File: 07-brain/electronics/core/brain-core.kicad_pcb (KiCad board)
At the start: 2 copper layers, 58 x 65 mm, 78 parts, among them J1 Conn_02x06_Odd_Even, J2 Conn_02x03_Odd_Even, J3 Conn_01x02, J4 Conn_02x04_Odd_Even, J5 Conn_02x02_Odd_Even, J6 Conn_02x05_Odd_Even, J7 Conn_02x05_Odd_Even, Q2 2N3819, Q4 BC848, U1 TL072, U2 TL072, U3 TL072, U4 NE5532, U5 TL072

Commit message: Design Brain/Core PCB
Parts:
- removed C17: 100n (foil), Capacitor_THT:C_Rect_L7.2mm_W2.5mm_P5.00mm_FKS2_FKP2_MKS2_MKP2
- removed C18: 1u (foil), Capacitor_THT:C_Rect_L7.0mm_W4.5mm_P5.00mm
- removed D_LIM_N1: Red LED, LED_THT:LED_D3.0mm
- removed D_LIM_P1: Red LED, LED_THT:LED_D5.0mm
- removed the G*** at (92.8, 84.6)
- removed the G*** at (82.2, 57.7)
- removed the J6 at (168.5, 98.0)
- removed Q2: 2N3819, Package_TO_SOT_THT:TO-92_Inline_Wide
- removed Q4: BC848, Package_TO_SOT_SMD:SOT-23
- removed the REF** at (125.1, 51.2)
- removed the REF** at (180.0, 87.8)
- removed RV_HEADPHONE_LIM1: 100k, Potentiometer_THT:Potentiometer_ACP_CA6-H2,5_Horizontal
- removed RV_LINE_OUT_LVL1: 10k, Potentiometer_THT:Potentiometer_ACP_CA6-H2,5_Horizontal
- removed TP1: MAX_LINEOUT, TestPoint:TestPoint_THTPad_2.0x2.0mm_Drill1.0mm
- removed TP2: MAINOUT, TestPoint:TestPoint_THTPad_2.0x2.0mm_Drill1.0mm
- removed TP3: PHONES_OUT, TestPoint:TestPoint_THTPad_2.0x2.0mm_Drill1.0mm
- added D5: BAT54S, Package_TO_SOT_SMD:SOT-23, F.Cu at (161.3, 88.1)
- added D6: BAT54S, Package_TO_SOT_SMD:SOT-23, F.Cu at (168.0, 88.0)
- added G***: LOGO, Shmoergh_Logo:Gyeszno, F.Cu at (202.0, 31.0)
- added G***: LOGO, Shmoergh_Logo:Gyeszno, B.Cu at (105.0, 126.0)
- added J10: Conn_01x02, Connector_PinHeader_2.54mm:PinHeader_1x02_P2.54mm_Vertical, F.Cu at (180.0, 52.6)
- added J7: Conn_02x05_Odd_Even, Connector_PinHeader_2.54mm:PinHeader_2x05_P2.54mm_Vertical, F.Cu at (161.0, 96.5)
- added J8: Conn_02x03_Odd_Even, Connector_PinHeader_2.54mm:PinHeader_2x03_P2.54mm_Vertical, F.Cu at (136.0, 152.0)
- added NT1: NetTie_2, NetTie:NetTie-2_SMD_Pad2.0mm, F.Cu at (160.2, 79.6)
- added Q1: MMBT3904, Package_TO_SOT_SMD:SOT-23, F.Cu at (175.1, 58.0)
- added Q3: MMBT3904, Package_TO_SOT_SMD:SOT-23, F.Cu at (171.0, 53.8)
- added Q6: MMBT3904, Package_TO_SOT_SMD:SOT-23, F.Cu at (163.9, 48.3)
- added Q7: MMBT3904, Package_TO_SOT_SMD:SOT-23, F.Cu at (159.1, 47.9)
- added R28: 33k, Resistor_SMD:R_0603_1608Metric, F.Cu at (139.8, 111.3)
- added R29: 33k, Resistor_SMD:R_0603_1608Metric, F.Cu at (155.0, 111.5)
- added R30: 100k, Resistor_SMD:R_0603_1608Metric, F.Cu at (149.8, 114.4)
- added R31: 100k, Resistor_SMD:R_0603_1608Metric, F.Cu at (165.1, 114.6)
- added R32: 100k, Resistor_SMD:R_0603_1608Metric, F.Cu at (149.8, 112.8)
- added R33: 100k, Resistor_SMD:R_0603_1608Metric, F.Cu at (165.1, 113.0)
- added R34: 1k, Resistor_SMD:R_0603_1608Metric, F.Cu at (149.8, 111.1)
- added R35: 1k, Resistor_SMD:R_0603_1608Metric, F.Cu at (165.1, 111.4)
- added REF**: ToolingHole_1.152mm, MountingHole:ToolingHole_1.152mm, F.Cu at (117.0, 110.0)
- added REF**: ToolingHole_1.152mm, MountingHole:ToolingHole_1.152mm, F.Cu at (116.9, 113.0)
- added REF**: ToolingHole_1.152mm, MountingHole:ToolingHole_1.152mm, F.Cu at (120.0, 110.0)
- added U10: 74HC4051, Package_SO:SOIC-16_3.9x9.9mm_P1.27mm, F.Cu at (154.1, 90.1)
- added U6: MCP4822, Package_SO:SOIC-8_3.9x4.9mm_P1.27mm, F.Cu at (129.1, 122.4)
- added U7: 74HC4053B, Package_SO:SOIC-16_3.9x9.9mm_P1.27mm, F.Cu at (133.3, 111.9)
- added U8: TL072, Package_SO:SOIC-8_3.9x4.9mm_P1.27mm, F.Cu at (144.5, 112.8)
- added U9: TL072, Package_SO:SOIC-8_3.9x4.9mm_P1.27mm, F.Cu at (159.7, 112.8)
- C1: value 100n -> 10u; footprint Capacitor_SMD:C_0603_1608Metric -> Capacitor_SMD:CP_Elec_4x5.4
- C10, C11: value 100n -> 22p
- C14: value 1u -> 100n; footprint Capacitor_SMD:C_0603_1608Metric_Pad1.08x0.95mm_HandSolder -> Capacitor_SMD:C_0603_1608Metric
- C15: value 100p -> 100n
- C16: value 100n (foil) -> 100n; footprint Capacitor_THT:C_Rect_L7.2mm_W2.5mm_P5.00mm_FKS2_FKP2_MKS2_MKP2 -> Capacitor_SMD:C_0603_1608Metric
- C2: value 100n -> 330n; footprint Capacitor_SMD:C_0603_1608Metric -> Capacitor_SMD:C_0603_1608Metric_Pad1.08x0.95mm_HandSolder
- C4, C5: value 100n -> 100u; footprint Capacitor_SMD:C_0603_1608Metric -> Capacitor_SMD:CP_Elec_6.3x7.7
- C7: value 22n-47n (foil) -> 100n; footprint Capacitor_THT:C_Rect_L7.0mm_W2.5mm_P5.00mm -> Capacitor_SMD:C_0603_1608Metric
- C8, C9: value 100u -> 100n; footprint Capacitor_SMD:CP_Elec_6.3x7.7 -> Capacitor_SMD:C_0603_1608Metric
- D3: value 1N4148 -> 1N5817; footprint Diode_SMD:D_SOD-123 -> Diode_SMD:D_SOD-323
- D4: value 1N4148 -> BAT54W; footprint Diode_SMD:D_SOD-123 -> Package_TO_SOT_SMD:SOT-23
- J1: value Conn_02x06_Odd_Even -> Conn_02x03_Odd_Even; footprint Connector_PinHeader_2.54mm:PinHeader_2x06_P2.54mm_Vertical -> Connector_PinHeader_2.54mm:PinHeader_2x03_P2.54mm_Vertical
- J2: value Conn_02x03_Odd_Even -> Conn_02x02_Odd_Even; footprint Connector_PinHeader_2.54mm:PinHeader_2x03_P2.54mm_Vertical -> Connector_PinHeader_2.54mm:PinHeader_2x02_P2.54mm_Vertical
- J3: value Conn_01x02 -> Conn_02x02_Odd_Even; footprint Connector_PinHeader_2.54mm:PinHeader_1x02_P2.54mm_Vertical -> Connector_PinHeader_2.54mm:PinHeader_2x02_P2.54mm_Vertical
- J4: value Conn_02x04_Odd_Even -> Conn_02x03_Odd_Even; footprint Connector_PinHeader_2.54mm:PinHeader_2x04_P2.54mm_Vertical -> Connector_PinHeader_2.54mm:PinHeader_2x03_P2.54mm_Vertical
- J5: value Conn_02x02_Odd_Even -> Conn_01x02; footprint Connector_PinHeader_2.54mm:PinHeader_2x02_P2.54mm_Vertical -> Connector_PinHeader_2.54mm:PinHeader_1x02_P2.54mm_Vertical
- R1: value 33k -> 100k
- R10: value 100k -> 68k; footprint Resistor_SMD:R_0603_1608Metric_Pad0.98x0.95mm_HandSolder -> Resistor_SMD:R_0603_1608Metric
- R11: value 4.7k -> 68k
- R12: value 150 -> 1k
- R14, R15: value 100 -> 100k
- R16: value 1M -> 100k
- R17: value 1k -> 100k
- R18, R20: value 10k -> 100k
- R22, R23: value 100k -> 1k
- R24: value 47k -> 100k
- R25: value 1k -> 120k
- R26: value 12k -> 100k
- R27: value 47k -> 120k
- R3: value 100k -> 10k
- R4: value 100k -> 7.5k
- R5: value 100k -> 2.2k
- R6: value 100k -> 120
- U1: value TL072 -> LM7805_TO220; footprint Package_SO:SOIC-8_3.9x4.9mm_P1.27mm -> Package_TO_SOT_THT:TO-220-3_Horizontal_TabDown
- U2: value TL072 -> 6N137; footprint Package_SO:SOIC-8_3.9x4.9mm_P1.27mm -> Package_SO:SOP-8_6.605x9.655mm_P2.54mm
- U3: value TL072 -> Pico; footprint Package_SO:SOIC-8_3.9x4.9mm_P1.27mm -> Module:RaspberryPi_Pico_Common_Unspecified
- U4: value NE5532 -> TL072
- moved J5 102.9 mm to (152.1, 148.9)
- moved C7 97.9 mm to (128.6, 133.2), turned to -90 degrees
- moved C4 91.8 mm to (159.8, 150.3), turned to 180 degrees
- moved C6 83.9 mm to (135.2, 140.9), turned to -90 degrees
- moved R18 81.3 mm to (145.8, 143.5)
- moved R8 80.9 mm to (132.5, 131.6), turned to -90 degrees
- moved D2 78.0 mm to (158.9, 144.5)
- moved R16 76.9 mm to (128.2, 142.7), turned to 90 degrees
- moved R9 75.4 mm to (145.5, 130.0), turned to -90 degrees
- moved R23 74.3 mm to (148.6, 144.3)
- moved R22 68.2 mm to (135.2, 144.2), turned to -90 degrees
- moved R21 68.1 mm to (145.8, 141.9), turned to 0 degrees
- moved C9 68.0 mm to (141.9, 133.2), turned to -90 degrees
- moved J4 68.0 mm to (168.0, 152.0), turned to 90 degrees
- moved C5 66.9 mm to (176.8, 120.7), turned to 180 degrees
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- renumbered J7 to J6
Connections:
- C10 pad 1: +12V -> Net-(U4A--)
- C10 pad 2: GND -> Net-(C10-Pad2)
- C11 pad 1: GND -> Net-(U5A--)
- C11 pad 2: -12V -> Net-(C11-Pad2)
- C12 pad 2: GND -> GNDA
- C13 pad 1: GND -> GNDA
- C14 pad 1: OUTPUT_VOL_2 -> +12V
- C14 pad 2: Net-(U5A-+) -> GNDA
- C15 pad 1: Net-(U5B--) -> GNDA
- C15 pad 2: OUTPUT_LINE_OUT -> -12V
- C16 pad 1: Net-(Q2-S) -> +3.3V
- C16 pad 2: GND -> GNDA
- C2 pad 1: GND -> +12V
- C2 pad 2: -12V -> GND
- C3 pad 1: +12V -> Net-(D1-A)
- C4 pad 1: GND -> +12V
- C4 pad 2: -12V -> GND
- C5 pad 1: +12V -> GND
- C5 pad 2: GND -> -12V
- C6 pad 1: GND -> +12V
- C6 pad 2: -12V -> GNDA
- C7 pad 1: LFO_TRI -> GNDA
- C7 pad 2: Net-(U3A--) -> -12V
- C8 pad 2: GND -> GNDA
- C9 pad 1: GND -> GNDA
- D1 pad 1: +12V -> +5V
- D2 pad 1: Net-(D2-K) -> +12V
- D2 pad 2: -12V -> Net-(D2-A)
- D3 pad 2: Net-(D3-A) -> -12V
- D4 pad 1: Net-(D4-K) -> MIDI_4R
- D4 pad 2: Net-(D4-A) -> unconnected-(D4-NC-Pad2)
- J1 pad 1: Net-(J1-Pin_1) -> LED_3
- J1 pad 2: Net-(J1-Pin_1) -> LED_4
- J1 pad 3: Net-(J1-Pin_3) -> LED_2
- J1 pad 4: Net-(J1-Pin_3) -> LED_5
- J1 pad 5: Net-(J1-Pin_5) -> LED_1
- J1 pad 6: Net-(J1-Pin_5) -> LED_6
- J2 pad 1: GND -> MIDI_5T
- J2 pad 2: +12V -> PULSE_IN
- J2 pad 3: GND -> MIDI_4R
- J2 pad 4: GND -> PULSE_OUT
- J3 pad 1: GND -> BTN_2
- J3 pad 2: GND -> BTN_LED_1
- J4 pad 1: CRUSH_OUT -> GND
- J4 pad 2: CRUSH_IN -> +12V
- J4 pad 3: CRUSH_TRIG -> GND
- J4 pad 4: CRUSH_TRIG_DEFAULT -> GND
- J4 pad 5: RV_CRUSH_1 -> -12V
- J4 pad 6: RV_CRUSH_3 -> GND
- J5 pad 1: LFO_SQR -> GND
- J5 pad 2: LFO_TRI -> GND
- J6 pad 1: Net-(D2-K) -> Net-(D3-K)
- J6 pad 10: Net-(D1-A) -> Net-(D2-A)
- J6 pad 2: Net-(D2-K) -> Net-(D3-K)
- J6 pad 9: Net-(D1-A) -> Net-(D2-A)
- R1 pad 1: GND -> PULSE_IN
- R1 pad 2: Net-(U2B--) -> Net-(Q1-B)
- R10 pad 1: GND -> Net-(U4A--)
- R10 pad 2: Net-(U5A-+) -> Net-(R10-Pad2)
- R11 pad 1: OUTPUT_LINE_OUT -> Net-(U5A--)
- R11 pad 2: Net-(U5B--) -> Net-(R11-Pad2)
- R12 pad 1: OUTPUT_LINE_OUT -> Net-(C10-Pad2)
- R12 pad 2: Net-(R12-Pad2) -> Net-(R10-Pad2)
- R13 pad 1: OUTPUT_LINE_OUT -> Net-(C11-Pad2)
- R13 pad 2: Net-(R13-Pad2) -> Net-(R11-Pad2)
- R14 pad 1: OUTPUT_PHONES_OUT -> Net-(R10-Pad2)
- R14 pad 2: Net-(U4B--) -> Net-(U4B-+)
- R15 pad 1: OUTPUT_PHONES_OUT -> Net-(R11-Pad2)
- R15 pad 2: Net-(U4A--) -> Net-(U5B-+)
- R16 pad 1: Net-(D4-A) -> GNDA
- R16 pad 2: Net-(Q2-D) -> Net-(U4B-+)
- R17 pad 1: Net-(U1B--) -> GNDA
- R17 pad 2: CRUSH_OUT -> Net-(U5B-+)
- R18 pad 1: Net-(U2A--) -> Net-(U7-A)
- R18 pad 2: CRUSH_TRIG_DEFAULT -> Net-(U5B--)
- R19 pad 1: RV_CRUSH_3 -> Net-(U4B--)
- R19 pad 2: CRUSH_TRIG_DEFAULT -> Net-(U7-B)
- R2 pad 1: LFO_RATE -> /GPIO_8
- R2 pad 2: Net-(U3A--) -> Net-(Q3-B)
- R20 pad 1: GND -> Net-(U4B--)
- R20 pad 2: RV_CRUSH_1 -> Net-(R20-Pad2)
- R21 pad 1: GND -> Net-(U5B--)
- R21 pad 2: Net-(D3-A) -> Net-(R21-Pad2)
- R22 pad 1: Net-(U2B--) -> Net-(R20-Pad2)
- R22 pad 2: +12V -> AUDIO_CV_OUT_2
- R23 pad 1: GND -> Net-(R21-Pad2)
- R23 pad 2: Net-(D3-K) -> AUDIO_CV_OUT_1
- R24 pad 1: GND -> +5V
- R24 pad 2: OUTPUT_DRIVE_1 -> Net-(U8A--)
- R25 pad 1: Net-(D_LIM_N1-K) -> AUDIO_CV_IN_1
- R25 pad 2: OUTPUT_DRIVE_3 -> Net-(U8A--)
- R26 pad 1: Net-(R26-Pad1) -> +5V
- R26 pad 2: LFO_SQR -> Net-(U9A--)
- R27 pad 1: LFO_SQR -> AUDIO_CV_IN_2
- R27 pad 2: GND -> Net-(U9A--)
- R3 pad 1: Net-(U3A-+) -> PULSE_OUT
- R3 pad 2: LFO_RATE -> +12V
- R4 pad 1: Net-(Q4-C) -> GND
- R4 pad 2: Net-(U3A--) -> PULSE_OUT
- R5 pad 1: Net-(U3A--) -> Net-(Q6-C)
- R5 pad 2: Net-(Q4-C) -> Net-(D4-K)
- R6 pad 1: Net-(U3A-+) -> MIDI_5T
- R6 pad 2: GND -> Net-(Q6-B)
- R7 pad 1: Net-(R26-Pad1) -> /GPIO_9
- R7 pad 2: Net-(Q4-B) -> +3.3V
- R8 pad 1: Net-(U3B-+) -> GNDA
- R8 pad 2: GND -> Net-(U4A--)
- R9 pad 1: Net-(U3B-+) -> GNDA
- R9 pad 2: Net-(R26-Pad1) -> Net-(U5A--)
- U1 pad 1: Net-(Q2-D) -> +12V
- U1 pad 2: Net-(Q2-D) -> GND
- U1 pad 3: CRUSH_IN -> Net-(D1-A)
- U2 pad 1: CRUSH_TRIG_DEFAULT -> unconnected-(U2-NC-Pad1)
- U2 pad 2: Net-(U2A--) -> Net-(D4-K)
- U2 pad 3: RV_CRUSH_2 -> Net-(Q7-C)
- U2 pad 4: -12V -> unconnected-(U2-NC-Pad4)
- U2 pad 5: Net-(D3-K) -> GND
- U2 pad 6: Net-(U2B--) -> /GPIO_9
- U2 pad 7: Net-(D4-K) -> unconnected-(U2-EN-Pad7)
- U2 pad 8: +12V -> +3.3V
- U3 pad 1: LFO_TRI -> /MCU/UART_TX
- U3 pad 2: Net-(U3A--) -> /MCU/UART_RX
- U3 pad 3: Net-(U3A-+) -> GND
- U3 pad 4: -12V -> /GPIO_2
- U3 pad 5: Net-(U3B-+) -> /GPIO_3
- U3 pad 6: LFO_TRI -> /GPIO_4
- U3 pad 7: Net-(R26-Pad1) -> /GPIO_5
- U3 pad 8: +12V -> GND
- U4 pad 1: Net-(U4A--) -> Net-(C10-Pad2)
- U4 pad 5: Net-(U4A--) -> Net-(U4B-+)
- U4 pad 7: Net-(U4B--) -> Net-(R20-Pad2)
- U5 pad 1: OUTPUT_DRIVE_3 -> Net-(C11-Pad2)
- U5 pad 2: OUTPUT_DRIVE_1 -> Net-(U5A--)
- U5 pad 5: Net-(D_LIM_N1-K) -> Net-(U5B-+)
- U5 pad 7: Net-(R12-Pad2) -> Net-(R21-Pad2)
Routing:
- net +3.3V: track 0.00 -> 118.4 mm, vias 0 -> 10
- net /GPIO_2: track 0.00 -> 101.2 mm
- net /GPIO_3: track 0.00 -> 99.7 mm
- net +5V: track 0.00 -> 95.1 mm, vias 0 -> 4
- net /GPIO_5: track 0.00 -> 93.8 mm, vias 0 -> 1
- net /GPIO_6: track 0.00 -> 73.0 mm, vias 0 -> 1
- net CRUSH_TRIG_DEFAULT: track 68.6 -> 0.00 mm
- net /GPIO_7: track 0.00 -> 67.7 mm, vias 0 -> 1
- net Net-(U7-A): track 0.00 -> 63.9 mm, vias 0 -> 6
- net Net-(D_LIM_N1-K): track 62.1 -> 0.00 mm, vias 4 -> 0
- net OUTPUT_DRIVE_3: track 52.6 -> 0.00 mm, vias 2 -> 0
- net /GPIO_17: track 0.00 -> 47.0 mm
- net Net-(U7-B): track 0.00 -> 46.5 mm, vias 0 -> 2
- net /GPIO_16: track 0.00 -> 46.2 mm
- net RV_CRUSH_2: track 44.4 -> 0.00 mm
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- added copper zone on F.Cu, net GNDA
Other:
- board size 58 x 65 mm -> 58 x 110 mm
- board text added: "12V has to be connected on the UI board (or manually here)"
- board text added: "HM-02 Analog VCO Core V0.1 / 2025 July"
- board text removed: "+"
- board text removed: "12V"
- board text removed: "DEFAULTS"
- board text removed: "ENV"
- board text removed: "ENV GAIN"
- board text removed: "GATE"
- board text removed: "HM-05 ADSR VCA V0.1 / 2025 Aug"
- board text removed: "NC"
- board text removed: "TP(2xGND)"
- board text removed: "VCA COMP"
- board text removed: "VCV"
- board text removed: "VIN"
- board text removed: "VOUT"

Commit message: Brain PCB WIP
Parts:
- removed NT1: NetTie_2, NetTie:NetTie-2_SMD_Pad2.0mm
- moved J10 25.8 mm to (155.0, 46.0), turned to -90 degrees
- moved U6 19.0 mm to (139.9, 106.7)
- moved R25 15.4 mm to (150.8, 102.5)
- moved R19 8.89 mm to (128.1, 135.8)
- moved U7 5.63 mm to (131.4, 106.7), turned to 90 degrees
- moved U8 4.63 mm to (148.2, 115.5)
- moved C15 4.63 mm to (159.6, 118.9)
- moved R24 4.63 mm to (148.4, 111.1)
- moved R26 4.63 mm to (163.1, 111.1)
- moved R32 4.63 mm to (153.6, 115.5)
- moved U9 4.63 mm to (163.4, 115.5)
- moved C12 4.63 mm to (152.1, 112.0)
- moved C13 4.63 mm to (144.4, 118.8)
- moved C14 4.63 mm to (167.3, 112.1)
- moved R27 4.63 mm to (157.1, 114.2)
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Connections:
- C12 pad 2: GNDA -> GND
- C13 pad 1: GNDA -> GND
- C14 pad 2: GNDA -> GND
- C15 pad 1: GNDA -> GND
- C16 pad 2: GNDA -> GND
- C6 pad 2: GNDA -> GND
- C7 pad 1: GNDA -> GND
- C8 pad 2: GNDA -> GND
- C9 pad 1: GNDA -> GND
- D5 pad 1: GNDA -> GND
- D6 pad 1: GNDA -> GND
- J10 pad 2: +12V -> +3.3V
- R16 pad 1: GNDA -> GND
- R17 pad 1: GNDA -> GND
- R8 pad 1: GNDA -> GND
- R9 pad 1: GNDA -> GND
- U10 pad 1: GNDA -> GND
- U10 pad 12: GNDA -> GND
- U10 pad 2: GNDA -> GND
- U10 pad 4: GNDA -> GND
- U10 pad 5: GNDA -> GND
- U10 pad 6: GNDA -> GND
- U10 pad 7: GNDA -> GND
- U10 pad 8: GNDA -> GND
- U10 pad 9: GNDA -> GND
- U3 pad 33: GNDA -> GND
- U6 pad 5: GNDA -> GND
- U6 pad 7: GNDA -> GND
- U7 pad 12: GNDA -> GND
- U7 pad 2: GNDA -> GND
- U7 pad 3: GNDA -> GND
- U7 pad 4: GNDA -> GND
- U7 pad 5: GNDA -> GND
- U7 pad 6: GNDA -> GND
- U7 pad 7: GNDA -> GND
- U7 pad 8: GNDA -> GND
- U7 pad 9: GNDA -> GND
- U8 pad 3: GNDA -> GND
- U8 pad 5: GNDA -> GND
- U9 pad 3: GNDA -> GND
- U9 pad 5: GNDA -> GND
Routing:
- net GNDA: track 29.2 -> 0.00 mm, vias 14 -> 0
- net +12V: track 162.8 -> 190.7 mm, vias 3 -> 4
- net /GPIO_5: track 93.8 -> 72.5 mm
- net /GPIO_3: track 99.7 -> 78.8 mm
- net /GPIO_2: track 101.2 -> 80.7 mm
- net AUDIO_CV_IN_1: track 21.7 -> 2.70 mm
- net Net-(U4A-+): track 10.8 -> 27.0 mm
- net Net-(U7-A): track 63.9 -> 74.6 mm, vias 6 -> 2
- net Net-(U8A--): track 9.28 -> 18.0 mm
- net /GPIO_17: track 47.0 -> 38.7 mm
- net Net-(U7-B): track 46.5 -> 38.4 mm, vias 2 -> 0
- net /GPIO_16: track 46.2 -> 38.6 mm
- net -12V: track 130.7 -> 123.3 mm
- net /GPIO_7: track 67.7 -> 73.2 mm
- net Net-(U5A-+): track 21.4 -> 26.7 mm
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- removed copper zone on F.Cu, net GNDA

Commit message: Designed Brain UI PCB
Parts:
- added J_USB_C_BRKOUT1: Conn_01x05, Connector_PinHeader_2.54mm:PinHeader_1x05_P2.54mm_Vertical, F.Cu at (167.7, 68.3)
- added SW1: SW_SPST, Button_Switch_THT:SW_Tactile_SKHH_Angled, F.Cu at (179.1, 53.5)
- U3: moved to B.Cu
- moved R3 48.1 mm to (126.9, 54.7), turned to 180 degrees
- moved R4 48.1 mm to (126.9, 53.0), turned to 0 degrees
- moved D1 42.8 mm to (133.8, 90.7), turned to -90 degrees
- moved Q3 41.2 mm to (129.9, 56.7)
- moved J5 40.8 mm to (126.5, 117.0)
- moved C3 36.9 mm to (134.5, 95.0)
- moved U1 36.9 mm to (141.8, 94.2)
- moved C1 36.9 mm to (140.0, 89.9)
- moved C2 36.9 mm to (144.1, 93.3)
- moved R1 35.6 mm to (139.0, 52.8)
- moved Q1 34.0 mm to (141.1, 56.3), turned to 0 degrees
- moved J10 31.2 mm to (126.0, 57.5), turned to 0 degrees
- moved J2 27.1 mm to (141.5, 49.0), turned to 180 degrees
- moved J1 25.6 mm to (165.0, 49.5), turned to 90 degrees
- moved R28 24.3 mm to (167.3, 109.3)
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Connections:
- J1 pad 1: LED_3 -> LED_1
- J1 pad 2: LED_4 -> LED_6
- J1 pad 5: LED_1 -> LED_3
- J1 pad 6: LED_6 -> LED_4
- J3 pad 1: BTN_2 -> BTN_1
- J3 pad 2: BTN_LED_1 -> BTN_LED_2
- J3 pad 3: BTN_1 -> BTN_2
- J3 pad 4: BTN_LED_2 -> BTN_LED_1
- J7 pad 1: POT_3 -> POT_2
- J7 pad 10: AUDIO_CV_IN_1 -> AUDIO_CV_IN_2
- J7 pad 2: GND -> POT_3
- J7 pad 3: POT_2 -> POT_1
- J7 pad 5: POT_1 -> GND
- J7 pad 6: AUDIO_CV_IN_2 -> AUDIO_CV_IN_1
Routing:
- net /GPIO_26: track 5.31 -> 43.5 mm
- net +3.3V: track 119.0 -> 153.9 mm, vias 10 -> 4
- net /GPIO_17: track 38.7 -> 10.4 mm
- net +12V: track 190.7 -> 162.9 mm
- net Net-(U7-A): track 74.6 -> 48.4 mm, vias 2 -> 4
- net /GPIO_16: track 38.6 -> 13.1 mm
- net LED_1: track 33.4 -> 15.8 mm
- net Net-(U4A-+): track 27.0 -> 9.77 mm
- net LED_6: track 16.6 -> 33.8 mm
- net Net-(Q3-B): track 10.1 -> 26.8 mm
- net /GPIO_2: track 80.7 -> 66.6 mm
- net BTN_2: track 9.59 -> 22.7 mm
- net BTN_1: track 14.4 -> 27.3 mm
- net BTN_LED_1: track 9.59 -> 22.0 mm
- net /GPIO_7: track 73.2 -> 85.5 mm, vias 1 -> 0
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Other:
- board text added: "Adafruit 5978 USB-C breakout soldered to TP pads on Pico. TBD"
- board text added: "Bootsel button, soldered to TP pads on the Pico. TBD"
- board text added: "Pico should be soldered top facing downwards using low profile pin sockets and headers. This way the bootsel button is accessible and the USB-C breakout can be attached to TP pads."

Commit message: Added decoupling caps to DAC in Brain
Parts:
- added C17: 100n, Capacitor_SMD:C_0603_1608Metric, F.Cu at (135.0, 115.8)
- added C18: 10u, Capacitor_SMD:C_0603_1608Metric, F.Cu at (137.7, 115.4)
- J_USB_C_BRKOUT1: value Conn_01x05 -> Conn_02x05_Top_Bottom; footprint Connector_PinHeader_2.54mm:PinHeader_1x05_P2.54mm_Vertical -> Connector_PinHeader_2.54mm:PinHeader_2x05_P2.54mm_Vertical
- moved J_USB_C_BRKOUT1 2.71 mm to (165.0, 68.6)
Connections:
- J_USB_C_BRKOUT1 pad 1: unconnected-(J_USB_C_BRKOUT1-Pin_1-Pad1) -> Net-(J_USB_C_BRKOUT1-Pin_1)
- J_USB_C_BRKOUT1 pad 2: unconnected-(J_USB_C_BRKOUT1-Pin_2-Pad2) -> Net-(J_USB_C_BRKOUT1-Pin_1)
- J_USB_C_BRKOUT1 pad 3: unconnected-(J_USB_C_BRKOUT1-Pin_3-Pad3) -> Net-(J_USB_C_BRKOUT1-Pin_3)
- J_USB_C_BRKOUT1 pad 4: unconnected-(J_USB_C_BRKOUT1-Pin_4-Pad4) -> Net-(J_USB_C_BRKOUT1-Pin_3)
- J_USB_C_BRKOUT1 pad 5: unconnected-(J_USB_C_BRKOUT1-Pin_5-Pad5) -> Net-(J_USB_C_BRKOUT1-Pin_5)
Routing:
- net Net-(J_USB_C_BRKOUT1-Pin_7): track 0.00 -> 2.54 mm
- net Net-(J_USB_C_BRKOUT1-Pin_5): track 0.00 -> 2.54 mm
- net Net-(J_USB_C_BRKOUT1-Pin_3): track 0.00 -> 2.54 mm
- net Net-(J_USB_C_BRKOUT1-Pin_10): track 0.00 -> 2.54 mm
- net Net-(J_USB_C_BRKOUT1-Pin_1): track 0.00 -> 2.54 mm
- net GND: vias 50 -> 52

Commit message: Refined Brain PCBs
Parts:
- added G***: LOGO, Shmoergh_Logo:Gyeszno, F.Cu at (128.8, 108.6)
- added J9: Conn_01x02, Connector_PinHeader_2.54mm:PinHeader_1x02_P2.54mm_Vertical, F.Cu at (134.8, 90.6)
- moved G*** 99.8 mm to (159.6, 121.3)
- moved D1 2.75 mm to (131.9, 88.7)
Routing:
- net +12V: track 162.9 -> 173.9 mm
- net Net-(D1-A): track 5.23 -> 8.67 mm
- net +5V: track 103.1 -> 102.4 mm
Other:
- board text added: "(2x)+12V"
- board text added: "(2x)GND"
- board text added: "+12V"
- board text added: "3.3V"
- board text added: "Adafruit 5978 USB-C breakout"
- board text added: "BOOTSEL button"
- board text added: "Connect +12V here OR on the UI board (used for Pulse out)."

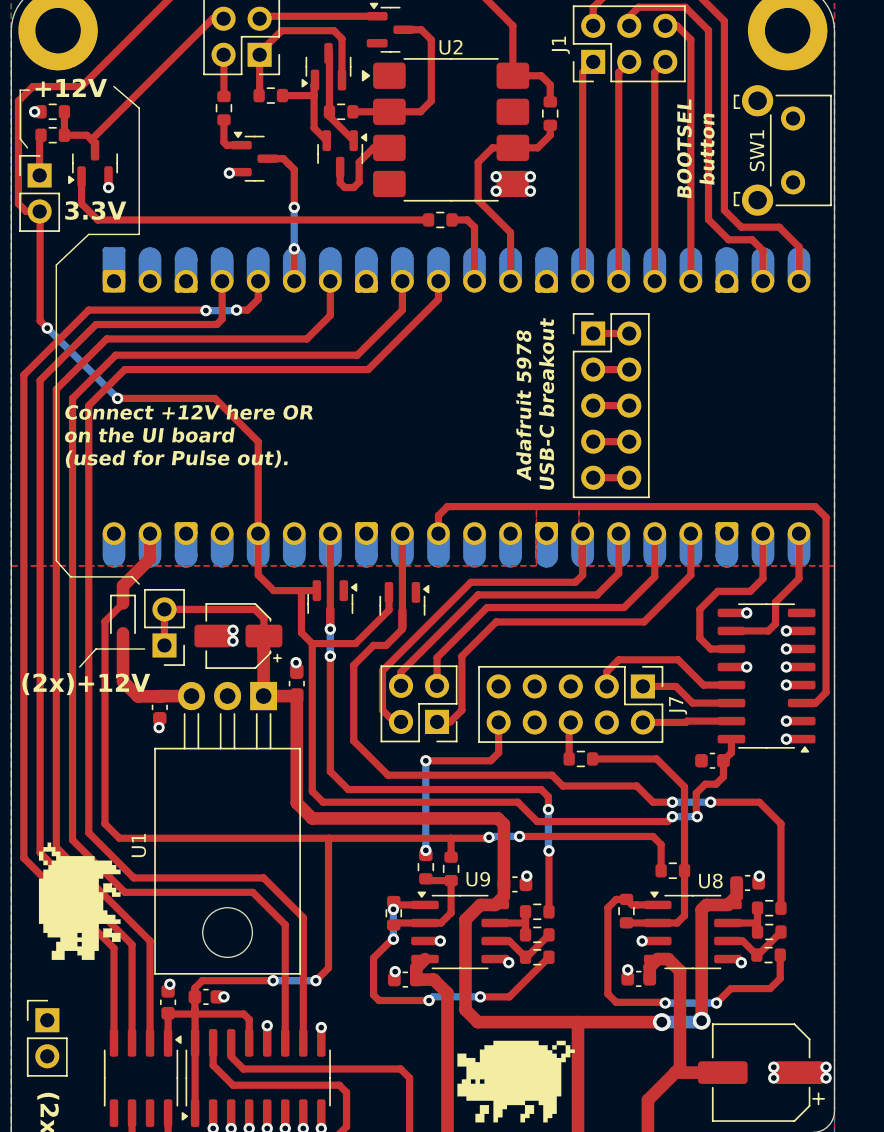
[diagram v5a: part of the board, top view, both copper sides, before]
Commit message: Added Adafruit USB-C breakout
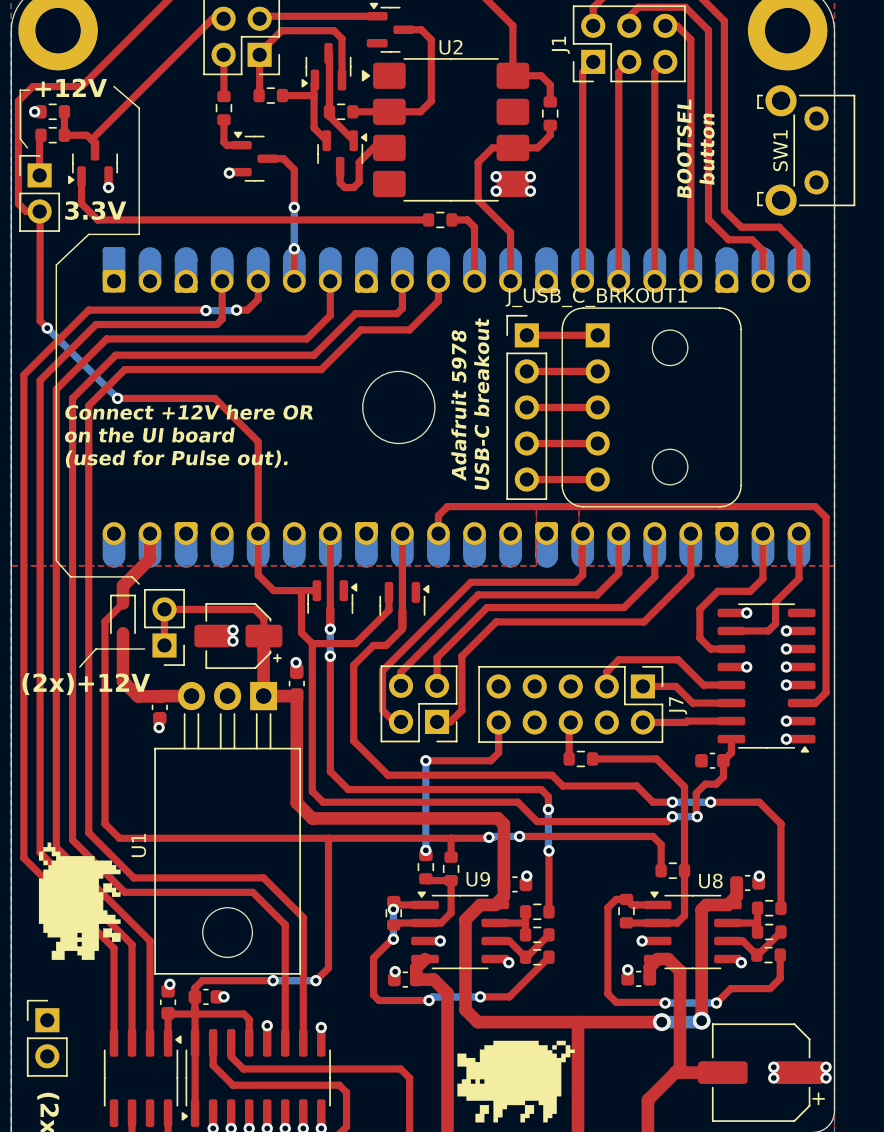
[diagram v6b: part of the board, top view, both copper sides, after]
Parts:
- added J_USB_C_BRKOUT_HEAD1: Conn_01x05, Connector_PinHeader_2.54mm:PinHeader_1x05_P2.54mm_Vertical, F.Cu at (160.3, 68.8)
- J_USB_C_BRKOUT1: value Conn_02x05_Top_Bottom -> Conn_01x05; footprint Connector_PinHeader_2.54mm:PinHeader_2x05_P2.54mm_Vertical -> Shmoergh_Custom_Footprints:Adafruit 5978 USB-C Breakout
- moved J_USB_C_BRKOUT1 5.22 mm to (165.3, 73.8)
- moved SW1 1.65 mm to (180.7, 53.5)
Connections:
- J_USB_C_BRKOUT1 pad 2: Net-(J_USB_C_BRKOUT1-Pin_1) -> Net-(J_USB_C_BRKOUT1-Pin_2)
- J_USB_C_BRKOUT1 pad 4: Net-(J_USB_C_BRKOUT1-Pin_3) -> Net-(J_USB_C_BRKOUT1-Pin_4)
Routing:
- net Net-(J_USB_C_BRKOUT1-Pin_4): track 0.00 -> 4.99 mm
- net Net-(J_USB_C_BRKOUT1-Pin_2): track 0.00 -> 4.99 mm
- net Net-(J_USB_C_BRKOUT1-Pin_7): track 2.54 -> 0.00 mm
- net Net-(J_USB_C_BRKOUT1-Pin_10): track 2.54 -> 0.00 mm
- net Net-(J_USB_C_BRKOUT1-Pin_5): track 2.54 -> 4.99 mm
- net Net-(J_USB_C_BRKOUT1-Pin_3): track 2.54 -> 4.99 mm
- net Net-(J_USB_C_BRKOUT1-Pin_1): track 2.54 -> 4.99 mm
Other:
- outline, holes or cut-outs redrawn
- board text added: "Adafruit 5978 USB-C breakout soldered to TP pads on Pico."
- board text added: "Bootsel button, soldered to TP pads on the Pico."
- board text removed: "Adafruit 5978 USB-C breakout soldered to TP pads on Pico. TBD"
- board text removed: "Bootsel button, soldered to TP pads on the Pico. TBD"
